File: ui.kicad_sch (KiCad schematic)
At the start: 42 parts, among them SW1 PEC11R-4215F-S0024, SW2 PEC11R-4215F-S0024, U10 BME280, U11 SN74HC14PWR, U12 LM35, U8 SN74AHCT244DBR, U9 24LC256-I/ST

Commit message: Board layout without errors
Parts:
- renumbered C24 to C30, C25 to C31, C26 to C32, C27 to C33, C28 to C34, C29 to C35, C30 to C36, C31 to C37, C32 to C38, C33 to C39, C34 to C40, C35 to C41, C36 to C42, C37 to C43, R10 to R12, R11 to R13, R12 to R14, R13 to R15, R14 to R16, R15 to R17, R16 to R18, R17 to R19, R18 to R20, R19 to R21, R20 to R22, R21 to R23, R22 to R24, R23 to R25, R24 to R26, R25 to R27, R26 to R28, U9 to U10, U10 to U11, U11 to U12, U12 to U13, U8 to U9

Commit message: Unavailable parts replaced, rotation issues fixed in library, except for U7
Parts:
- DS1: LCSC C17492463 -> Display: C17492463, Connector: C262557
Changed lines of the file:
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@@
 			)
 		)
-		(property "LCSC" "C17492463"
+		(property "LCSC" "Display: C17492463, Connector: C262557"
 			(at 212.09 101.854 0)
 			(hide yes)

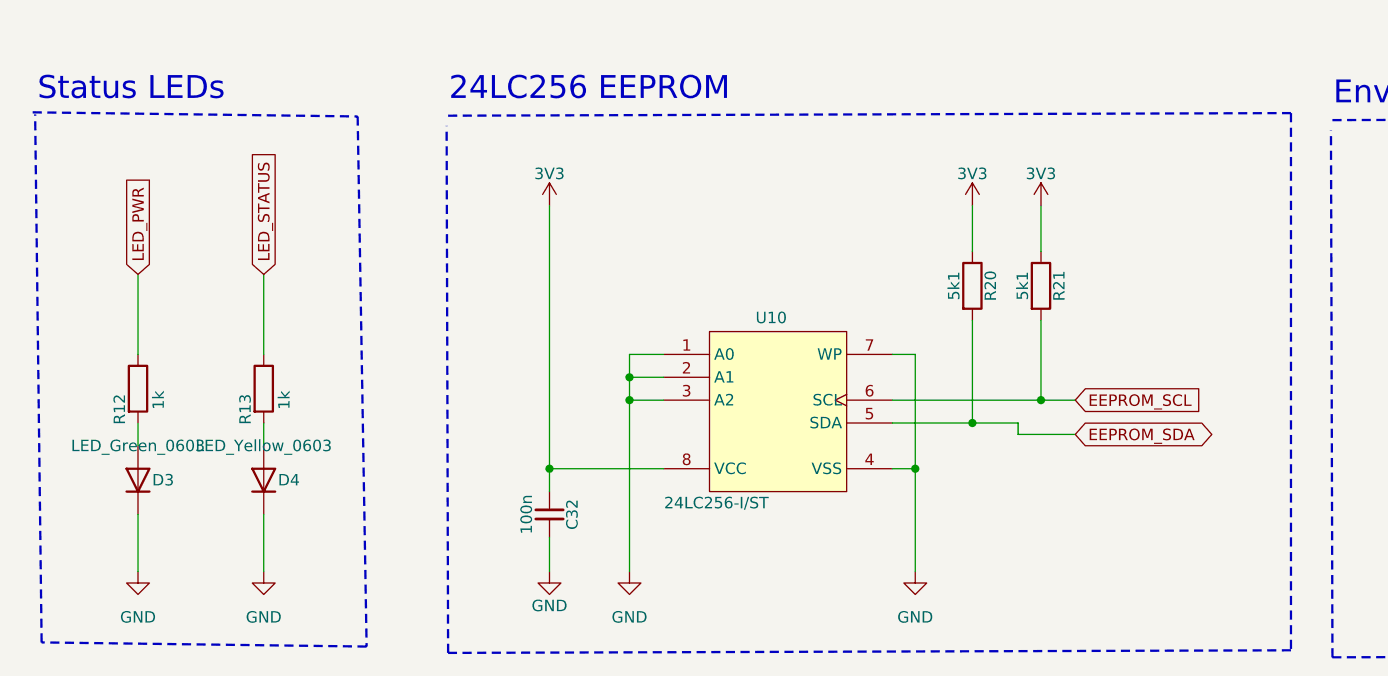
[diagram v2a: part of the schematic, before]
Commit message: Fix stock/pinout issues, re-export fabrication files, apply JLC rotation corrections
- Replace out-of-stock parts (D2/D3 LED, U5, U10) with in-stock JLCPCB
  alternatives; add D5-D12 protection diodes
- Fix U2/DW01A footprint rotation on PCB
- Re-export gerbers, drill files, and JLCSMT BOM/CPL from current design
- BOM/CPL: DS1 uses header connector LCSC number only (display bought
  separately), U13 (LM35) and mounting holes excluded as do-not-place
- CPL rotations for U7, U5, Q3, U2 corrected per known JLCPCB
  per-part orientation quirks (see sldrnrd_kicad_lib/JLC_ROTATION_OFFSETS.md)
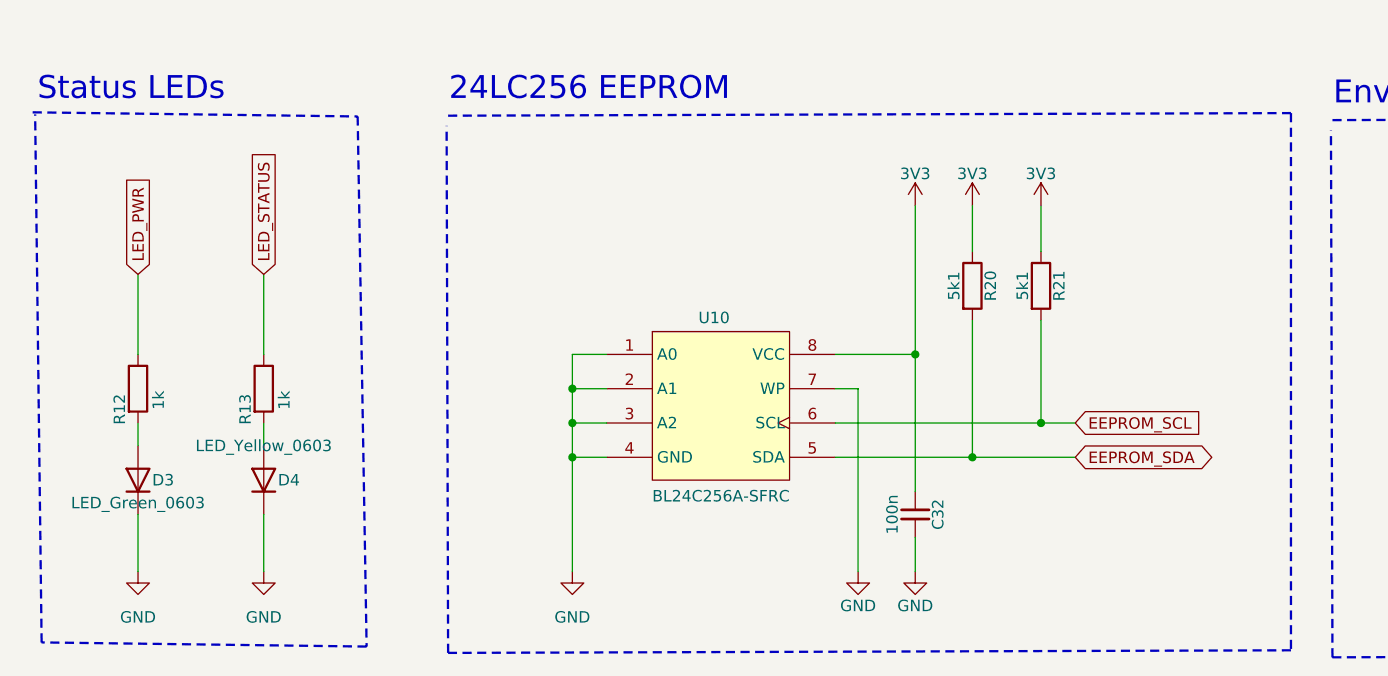
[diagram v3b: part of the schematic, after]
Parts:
- D3: symbol sldrnrd:LED/LED_Green_0603 -> sldrnrd:LED/LED_Green_0603_NationStar; LCSC C72043 -> C87326; MPN 19-217/GHC-YR1S2/3T -> NCD0603G2; Manufacturer EVERLIGHT -> NationStar
- U10: value 24LC256-I/ST -> BL24C256A-SFRC; symbol sldrnrd:Memory/EEPROM/24LC256-I_ST -> sldrnrd:Memory/EEPROM/BL24C256A-SFRC; LCSC C87823 -> C110276; MPN 24LC256-I/ST -> BL24C256A-SFRC; Manufacturer Microchip -> Shanghai Belling
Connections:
- net GND: now also D3.1 (K), D4.1 (K); no longer D3.2 (K), D4.2 (K)
- net at R12.2: now also D3.2 (A); no longer D3.1 (A)
- net at R13.2: now also D4.2 (A); no longer D4.1 (A)
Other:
- moved on the sheet: C32, U10

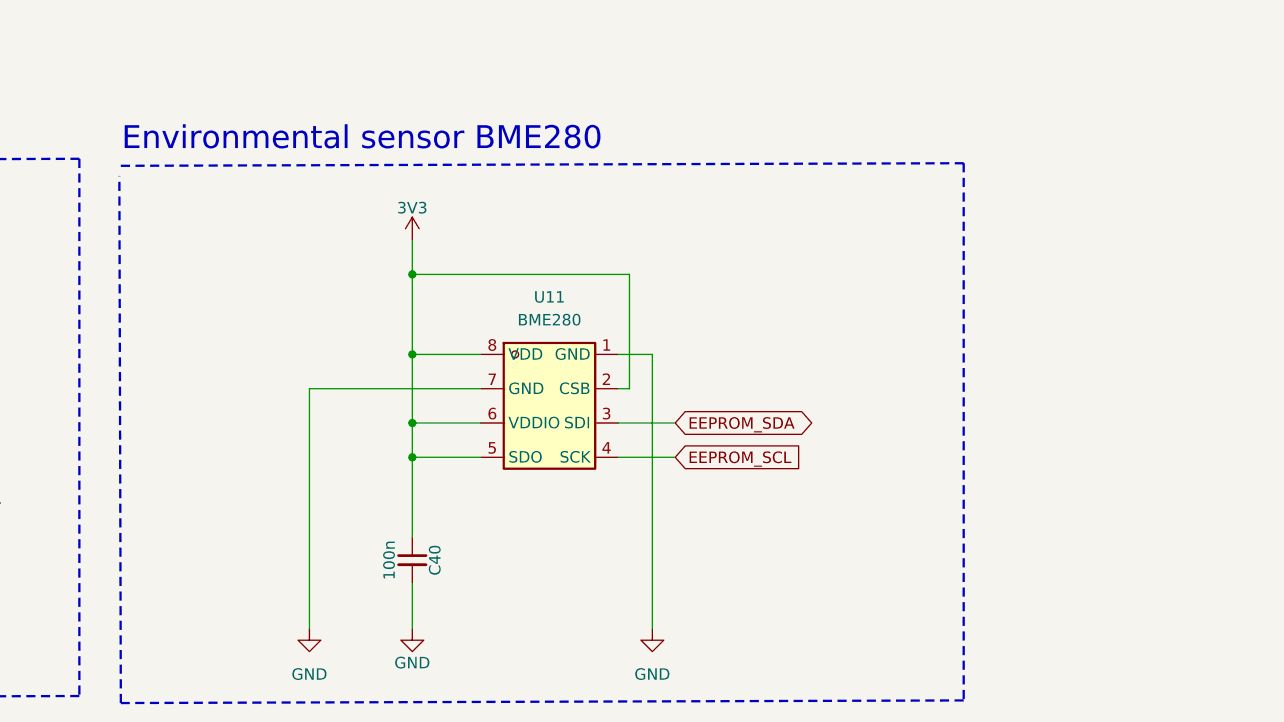
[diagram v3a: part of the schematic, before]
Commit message: Header for external BME280 module added, Keepout for BLE module fixed
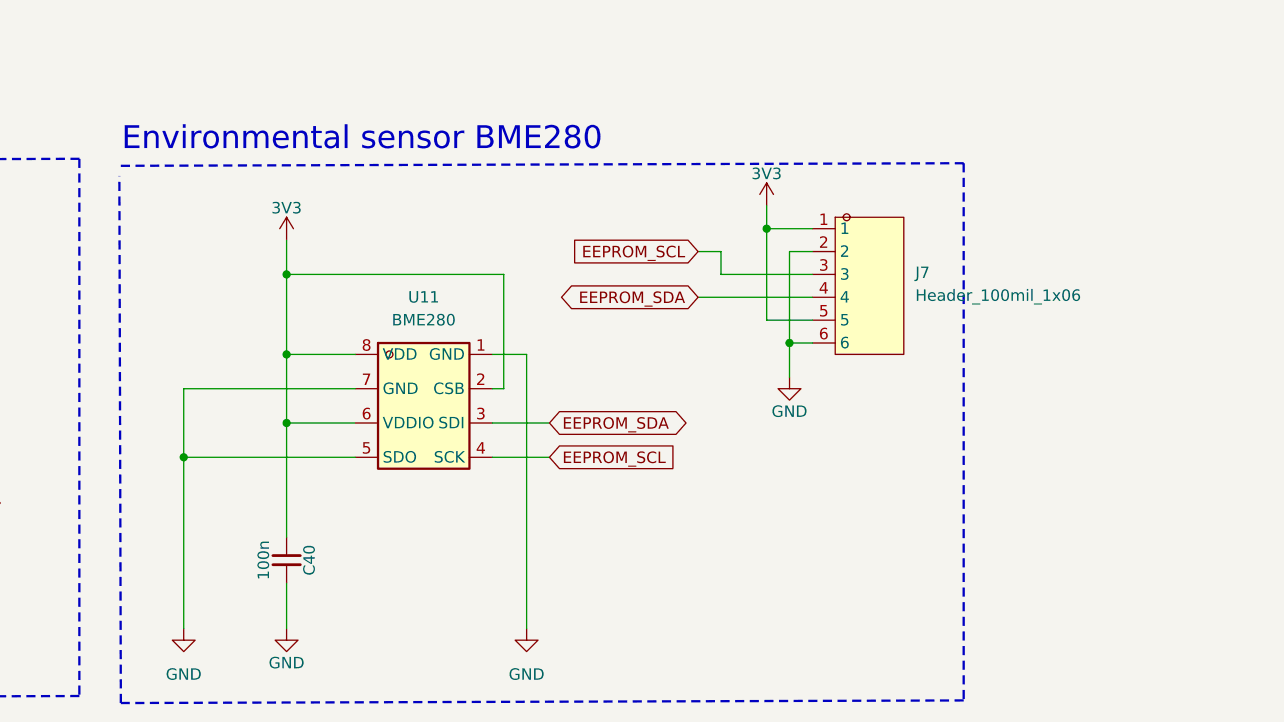
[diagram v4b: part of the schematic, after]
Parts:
- added J7: Header_100mil_1x06, sldrnrd:Header_100mil_1x06, symbol sldrnrd:Connector/100Mil/Header_100mil_1x06
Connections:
- net 3V3: now also J7.1, J7.5; no longer U11.5 (SDO)
- net EEPROM_SCL: now also J7.3
- net EEPROM_SDA: now also J7.4
- net GND: now also U11.5 (SDO), J7.2, J7.6
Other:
- moved on the sheet: C40, U11

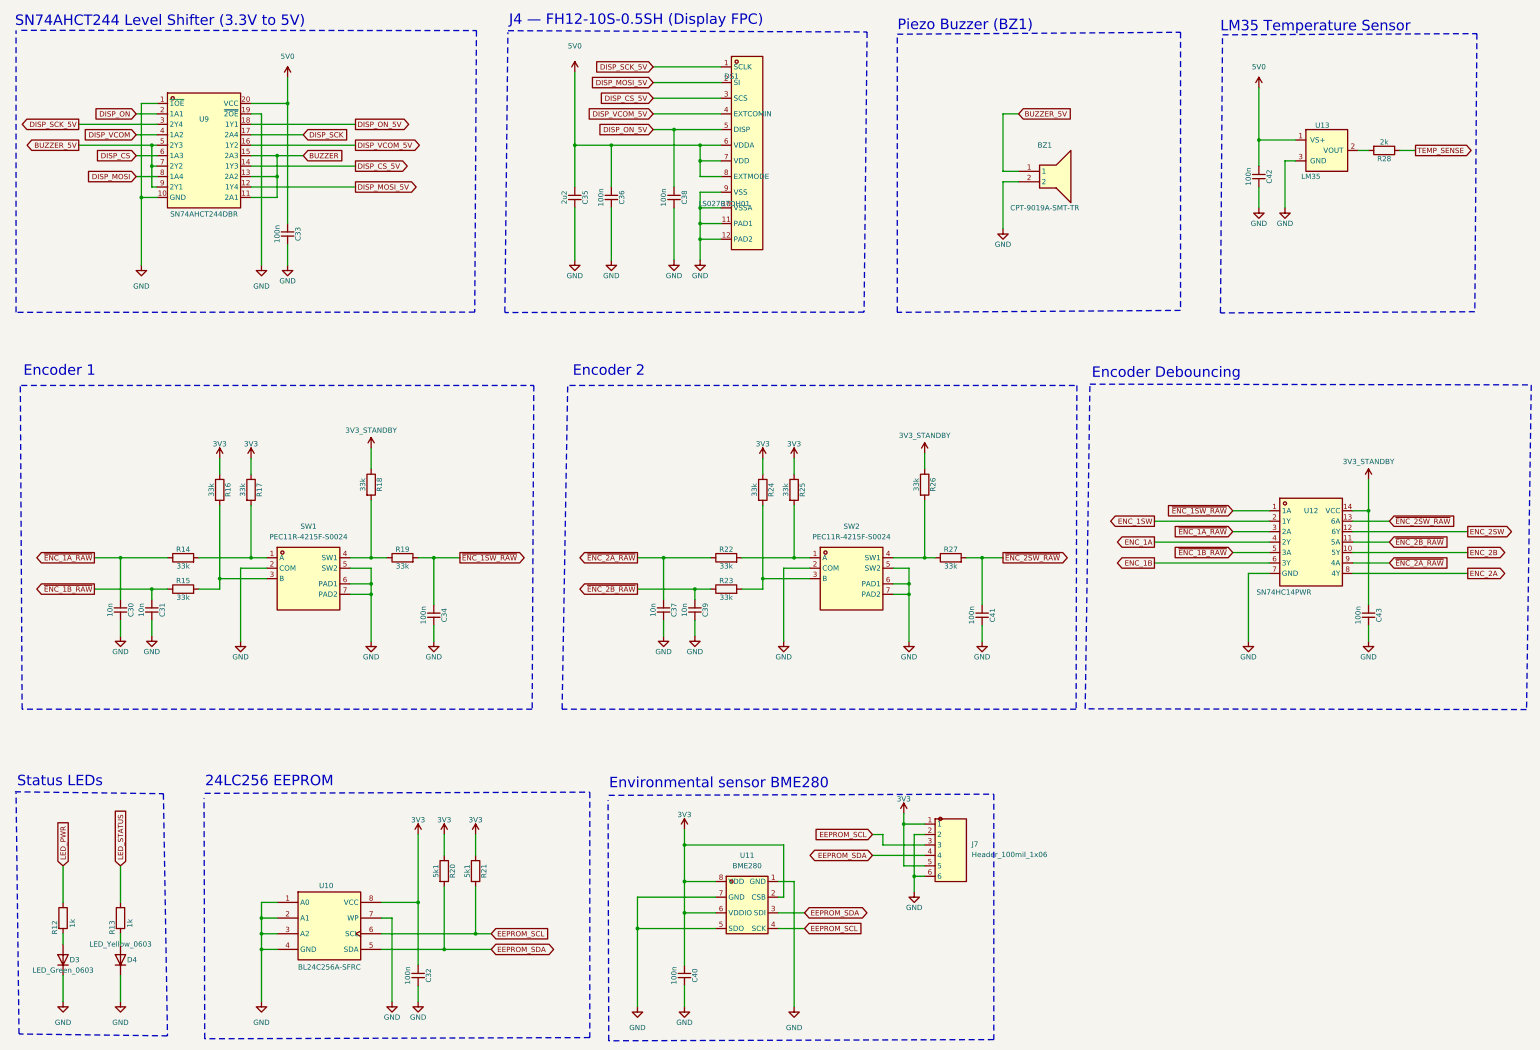
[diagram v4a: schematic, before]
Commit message: Debug headers for SPI1, SPI2 and SPI3 added
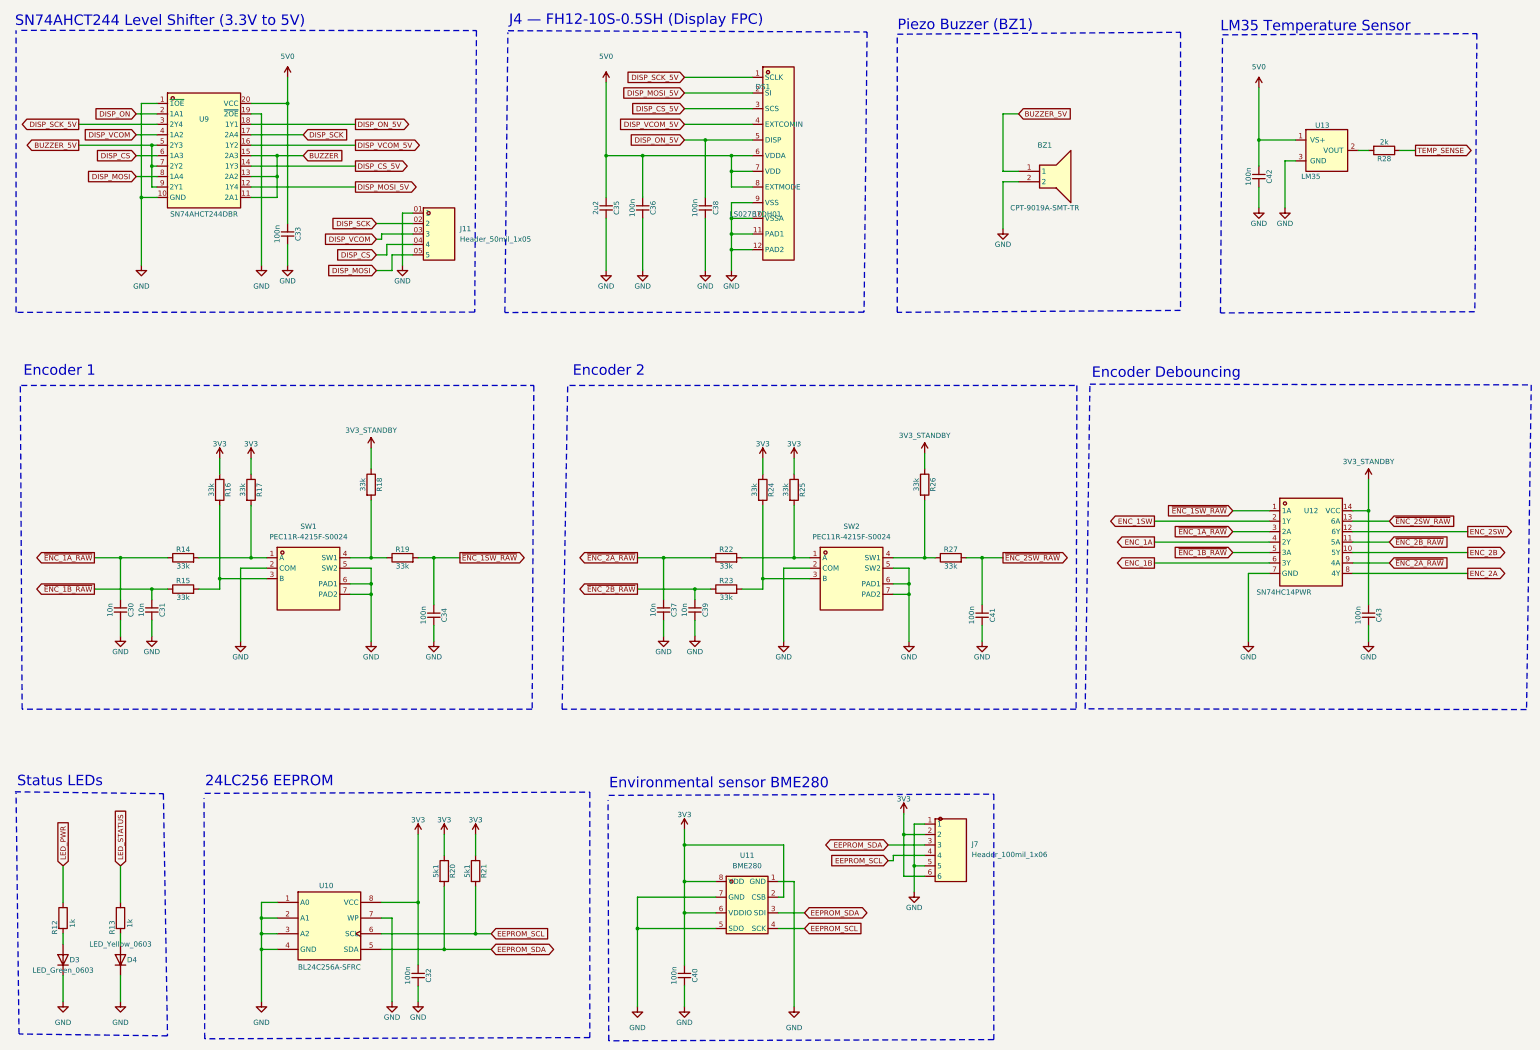
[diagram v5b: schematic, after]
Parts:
- added J11: Header_50mil_1x05, sldrnrd:Header_50mil_1x05, symbol sldrnrd:Connector/50Mil/Header_50mil_1x05
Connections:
- net 3V3: now also J7.2, J7.6; no longer J7.1, J7.5
- net DISP_CS: now also J11.04 (4)
- net DISP_MOSI: now also J11.05 (5)
- net DISP_SCK: now also J11.02 (2)
- net DISP_VCOM: now also J11.03 (3)
- net EEPROM_SCL: now also J7.4; no longer J7.3
- net EEPROM_SDA: now also J7.3; no longer J7.4
- net GND: now also J7.1, J7.5, J11.01 (1); no longer J7.2, J7.6
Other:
- moved on the sheet: C35, C36, C38, DS1

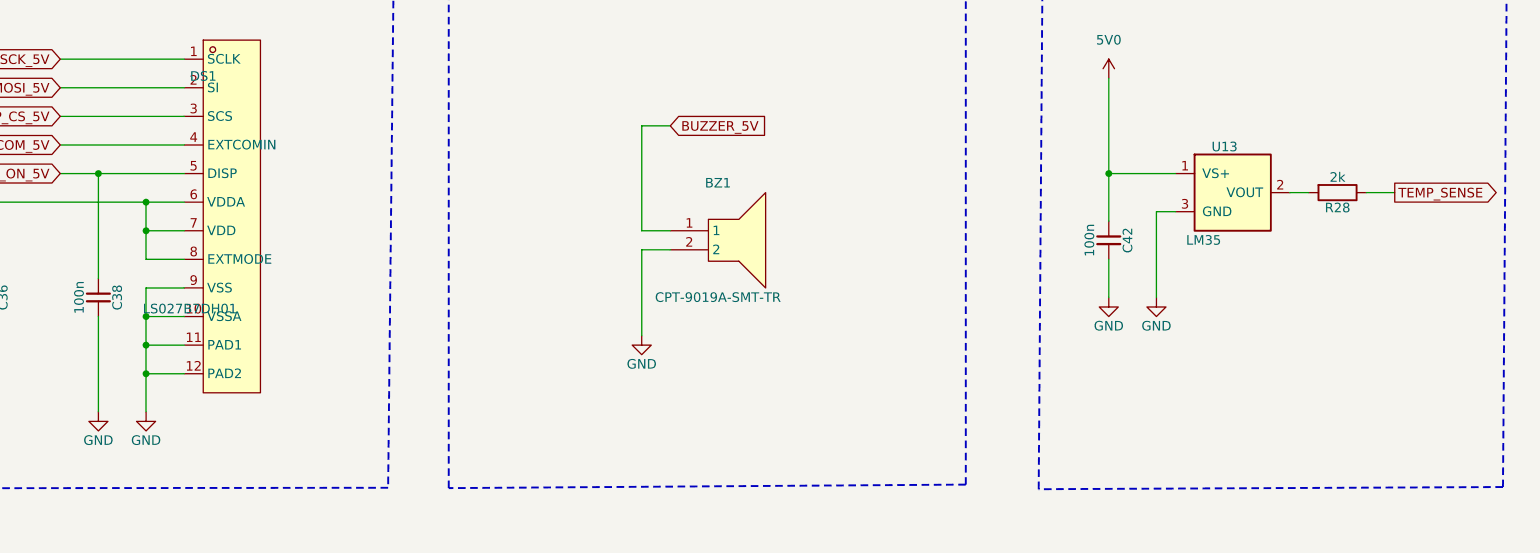
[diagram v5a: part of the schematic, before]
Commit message: Schematic checks, some smaller corrections, debug UART pinout corrected on programming header
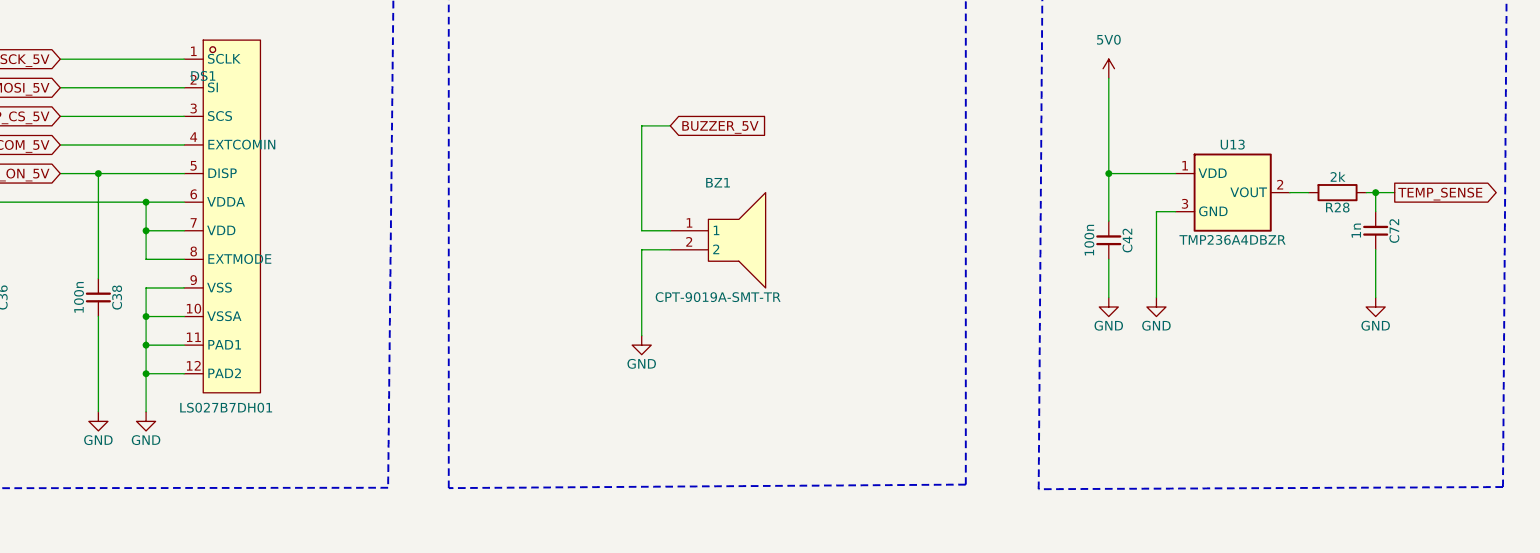
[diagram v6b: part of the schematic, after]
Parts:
- added C72: 1n, sldrnrd:C_0603, symbol sldrnrd:Capacitor/C0603_1n
- U13: value LM35 -> TMP236A4DBZR; symbol sldrnrd:Sensor/LM35 -> sldrnrd:Sensor/TMP236A4DBZR; LCSC C9900081740 -> C2872164; MPN (none) -> TMP236A4DBZR; Manufacturer (none) -> Texas Instruments
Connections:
- net GND: now also C72.2
- net TEMP_SENSE: now also C72.1

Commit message: Further checks. Capacitors unified to basic parts
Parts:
- C35: Dielectric X7R -> X5R; LCSC C126589 -> C377773; MPN GCM21BR71C225KA64L -> CL21A225KBQNNNE; Manufacturer Murata -> Samsung Electro-Mechanics; Voltage 16V -> 50V
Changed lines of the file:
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@@
 			)
 		)
-		(property "LCSC" "C126589"
+		(property "LCSC" "C377773"
 			(at 179.07 77.47 0)
 			(hide yes)
@@
 			)
 		)
-		(property "Dielectric" "X7R"
+		(property "Dielectric" "X5R"
 			(at 179.07 77.47 0)
 			(hide yes)
@@
 			)
 		)
-		(property "Voltage" "16V"
+		(property "Voltage" "50V"
 			(at 179.07 77.47 0)
 			(hide yes)
@@
 			)
 		)
-		(property "Manufacturer" "Murata"
+		(property "Manufacturer" "Samsung Electro-Mechanics"
 			(at 179.07 77.47 0)
 			(hide yes)
@@
 			)
 		)
-		(property "MPN" "GCM21BR71C225KA64L"
+		(property "MPN" "CL21A225KBQNNNE"
 			(at 179.07 77.47 0)
 			(hide yes)
@@
 		)
 	)
+	(embedded_fonts no)
 )
